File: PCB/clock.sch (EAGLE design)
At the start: 9 parts, among them IC1 74LS595N, IC2 74LS595N, IC3 74LS595N

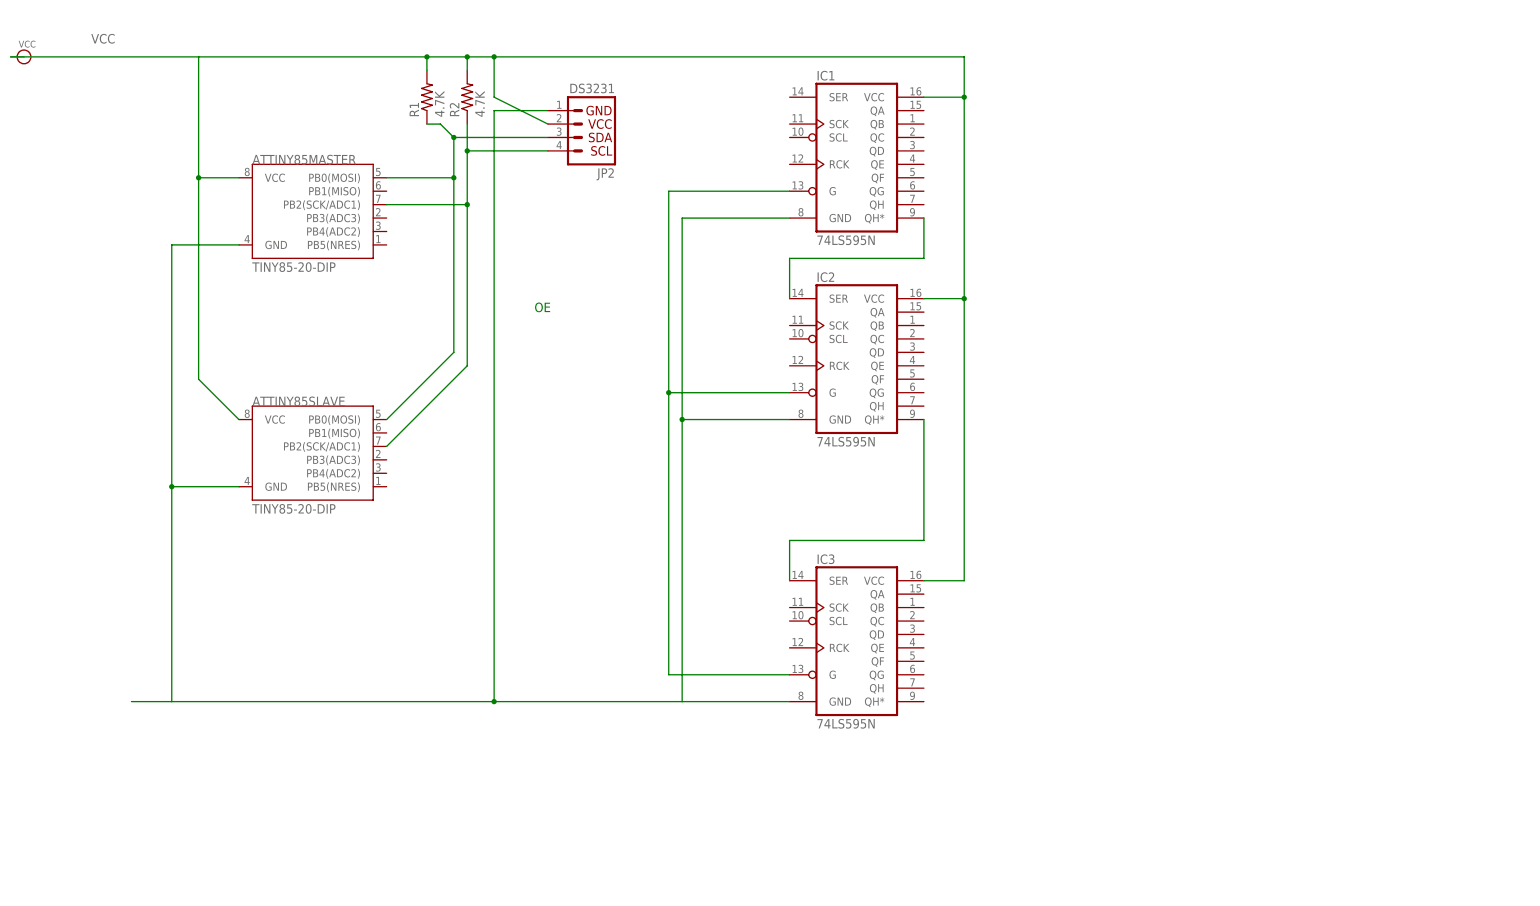
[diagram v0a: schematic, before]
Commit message: Updated the schematic for better readability
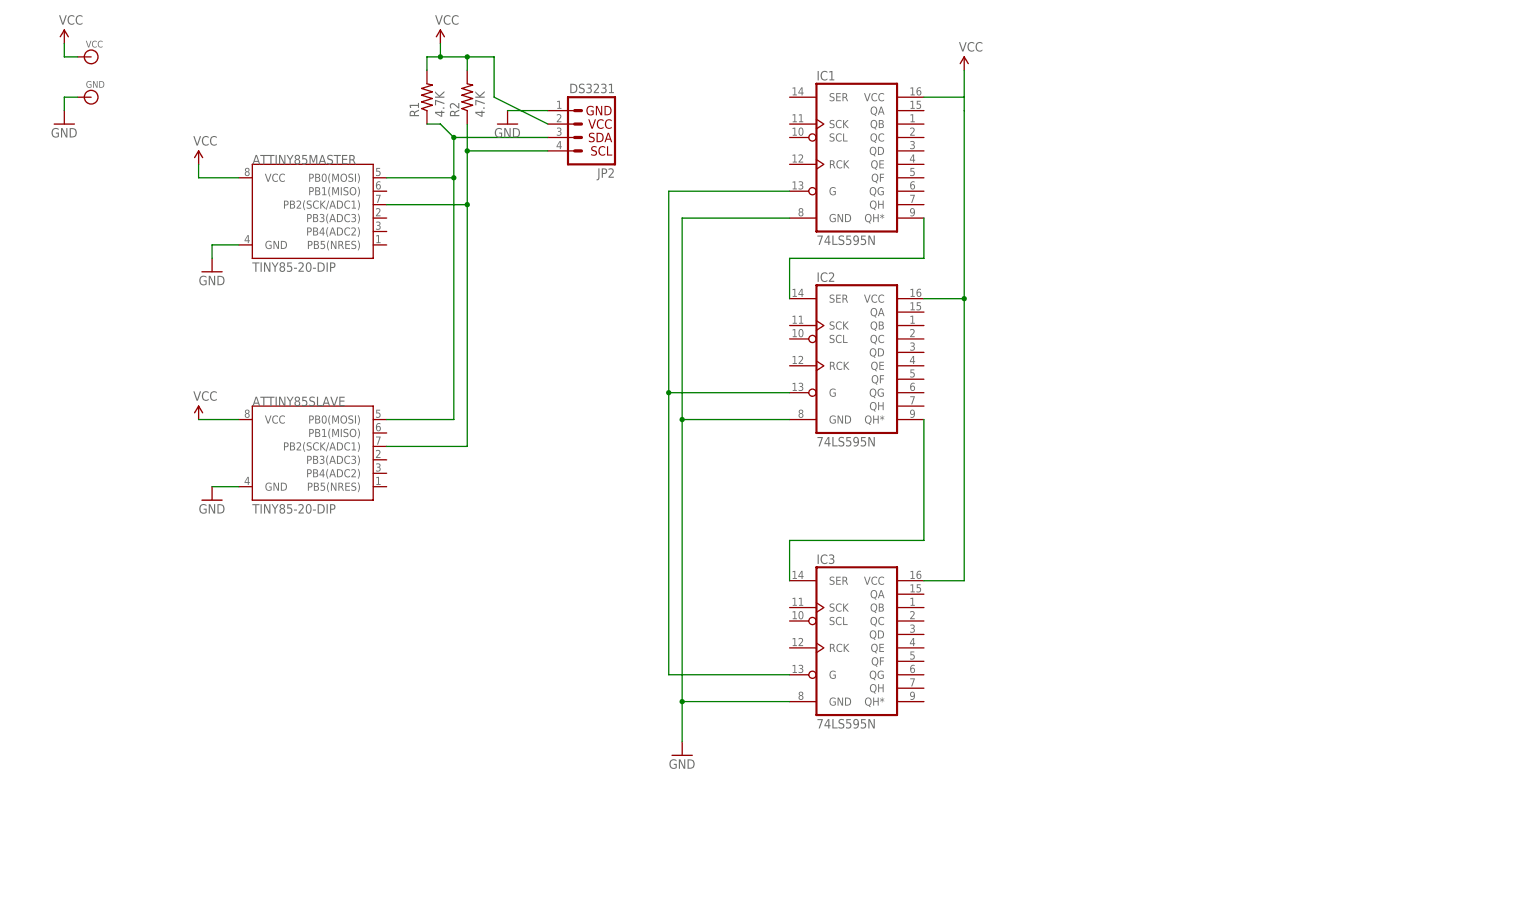
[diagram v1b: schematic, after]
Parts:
- added GND: (no value), SparkFun-Connectors:BANANA_CONN
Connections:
- net GND: now also GND.1
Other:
- note removed: "OE"
- moved on the sheet: VCC
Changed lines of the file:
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@@
 <part name="R1" library="SparkFun-Resistors" deviceset="RESISTOR" device="PTH-1/4W" value="4.7K"/>
 <part name="R2" library="SparkFun-Resistors" deviceset="RESISTOR" device="PTH-1/4W" value="4.7K"/>
+<part name="SUPPLY1" library="SparkFun-Aesthetics" deviceset="VCC" device=""/>
+<part name="SUPPLY2" library="SparkFun-Aesthetics" deviceset="VCC" device=""/>
+<part name="SUPPLY3" library="SparkFun-Aesthetics" deviceset="VCC" device=""/>
+<part name="SUPPLY4" library="SparkFun-Aesthetics" deviceset="VCC" device=""/>
+<part name="SUPPLY5" library="SparkFun-Aesthetics" deviceset="VCC" device=""/>
+<part name="GND1" library="SparkFun-Aesthetics" deviceset="GND" device=""/>
+<part name="GND2" library="SparkFun-Aesthetics" deviceset="GND" device=""/>
+<part name="GND3" library="SparkFun-Aesthetics" deviceset="GND" device=""/>
+<part name="GND4" library="SparkFun-Aesthetics" deviceset="GND" device=""/>
+<part name="GND5" library="SparkFun-Aesthetics" deviceset="GND" device=""/>
+<part name="GND" library="SparkFun-Connectors" deviceset="BANANA_CONN" device=""/>
 </parts>
 <sheets>
 <sheet>
 <plain>
-<text x="0" y="55.88" size="1.778" layer="91">OE</text>
 </plain>
 <instances>
@@
 <instance part="IC3" gate="A" x="58.42" y="-5.08"/>
 <instance part="ATTINY85MASTER" gate="G$1" x="-40.64" y="73.66"/>
-<instance part="VCC" gate="G$1" x="-96.52" y="104.14"/>
+<instance part="VCC" gate="G$1" x="-83.82" y="104.14"/>
 <instance part="JP2" gate="G$1" x="12.7" y="96.52" rot="R180"/>
 <instance part="ATTINY85SLAVE" gate="G$1" x="-40.64" y="27.94"/>
 <instance part="R1" gate="G$1" x="-20.32" y="96.52" rot="R90"/>
 <instance part="R2" gate="G$1" x="-12.7" y="96.52" rot="R90"/>
+<instance part="SUPPLY1" gate="G$1" x="-63.5" y="35.56"/>
+<instance part="SUPPLY2" gate="G$1" x="-17.78" y="106.68"/>
+<instance part="SUPPLY3" gate="G$1" x="81.28" y="101.6"/>
+<instance part="SUPPLY4" gate="G$1" x="-88.9" y="106.68"/>
+<instance part="SUPPLY5" gate="G$1" x="-63.5" y="83.82"/>
+<instance part="GND1" gate="1" x="-60.96" y="20.32"/>
+<instance part="GND2" gate="1" x="-60.96" y="63.5"/>
+<instance part="GND3" gate="1" x="-5.08" y="91.44"/>
+<instance part="GND4" gate="1" x="-88.9" y="91.44"/>
+<instance part="GND5" gate="1" x="27.94" y="-27.94"/>
+<instance part="GND" gate="G$1" x="-83.82" y="96.52"/>
 </instances>
 <busses>
@@
 <pinref part="IC1" gate="A" pin="VCC"/>
 <wire x1="73.66" y1="96.52" x2="81.28" y2="96.52" width="0.1524" layer="91"/>
-<wire x1="81.28" y1="96.52" x2="81.28" y2="58.42" width="0.1524" layer="91"/>
+<wire x1="81.28" y1="96.52" x2="81.28" y2="93.98" width="0.1524" layer="91"/>
 <junction x="81.28" y="58.42"/>
-<wire x1="81.28" y1="96.52" x2="81.28" y2="104.14" width="0.1524" layer="91"/>
-<junction x="81.28" y="96.52"/>
-<wire x1="81.28" y1="104.14" x2="-7.62" y2="104.14" width="0.1524" layer="91"/>
-<pinref part="ATTINY85MASTER" gate="G$1" pin="VCC"/>
+<pinref part="SUPPLY3" gate="G$1" pin="VCC"/>
+<wire x1="81.28" y1="93.98" x2="81.28" y2="58.42" width="0.1524" layer="91"/>
+<wire x1="81.28" y1="101.6" x2="81.28" y2="96.52" width="0.1524" layer="91"/>
+</segment>
+<segment>
+<pinref part="VCC" gate="G$1" pin="1"/>
+<pinref part="SUPPLY4" gate="G$1" pin="VCC"/>
+<wire x1="-86.36" y1="104.14" x2="-88.9" y2="104.14" width="0.1524" layer="91"/>
+<wire x1="-88.9" y1="104.14" x2="-88.9" y2="106.68" width="0.1524" layer="91"/>
+</segment>
+<segment>
+<pinref part="JP2" gate="G$1" pin="2"/>
+<wire x1="-7.62" y1="96.52" x2="2.54" y2="91.44" width="0.1524" layer="91"/>
+<wire x1="-7.62" y1="104.14" x2="-7.62" y2="96.52" width="0.1524" layer="91"/>
 <wire x1="-7.62" y1="104.14" x2="-12.7" y2="104.14" width="0.1524" layer="91"/>
-<wire x1="-12.7" y1="104.14" x2="-20.32" y2="104.14" width="0.1524" layer="91"/>
-<wire x1="-20.32" y1="104.14" x2="-63.5" y2="104.14" width="0.1524" layer="91"/>
-<wire x1="-63.5" y1="104.14" x2="-99.06" y2="104.14" width="0.1524" layer="91"/>
-<wire x1="-55.88" y1="81.28" x2="-63.5" y2="81.28" width="0.1524" layer="91"/>
-<wire x1="-63.5" y1="81.28" x2="-63.5" y2="104.14" width="0.1524" layer="91"/>
-<pinref part="VCC" gate="G$1" pin="1"/>
-<label x="-83.82" y="106.68" size="1.778" layer="95"/>
-<pinref part="JP2" gate="G$1" pin="2"/>
-<wire x1="-7.62" y1="104.14" x2="-7.62" y2="96.52" width="0.1524" layer="91"/>
-<wire x1="-7.62" y1="96.52" x2="2.54" y2="91.44" width="0.1524" layer="91"/>
-<junction x="-7.62" y="104.14"/>
-<pinref part="ATTINY85SLAVE" gate="G$1" pin="VCC"/>
-<wire x1="-63.5" y1="81.28" x2="-63.5" y2="43.18" width="0.1524" layer="91"/>
-<wire x1="-63.5" y1="43.18" x2="-55.88" y2="35.56" width="0.1524" layer="91"/>
-<junction x="-63.5" y="81.28"/>
 <pinref part="R2" gate="G$1" pin="2"/>
 <wire x1="-12.7" y1="101.6" x2="-12.7" y2="104.14" width="0.1524" layer="91"/>
 <junction x="-12.7" y="104.14"/>
+<wire x1="-12.7" y1="104.14" x2="-17.78" y2="104.14" width="0.1524" layer="91"/>
 <pinref part="R1" gate="G$1" pin="2"/>
+<wire x1="-17.78" y1="104.14" x2="-20.32" y2="104.14" width="0.1524" layer="91"/>
 <wire x1="-20.32" y1="101.6" x2="-20.32" y2="104.14" width="0.1524" layer="91"/>
-<junction x="-20.32" y="104.14"/>
+<pinref part="SUPPLY2" gate="G$1" pin="VCC"/>
+<wire x1="-17.78" y1="106.68" x2="-17.78" y2="104.14" width="0.1524" layer="91"/>
+<junction x="-17.78" y="104.14"/>
+</segment>
+<segment>
+<pinref part="ATTINY85MASTER" gate="G$1" pin="VCC"/>
+<wire x1="-55.88" y1="81.28" x2="-63.5" y2="81.28" width="0.1524" layer="91"/>
+<pinref part="SUPPLY5" gate="G$1" pin="VCC"/>
+<wire x1="-63.5" y1="83.82" x2="-63.5" y2="81.28" width="0.1524" layer="91"/>
+</segment>
+<segment>
+<pinref part="SUPPLY1" gate="G$1" pin="VCC"/>
+<pinref part="ATTINY85SLAVE" gate="G$1" pin="VCC"/>
+<wire x1="-63.5" y1="35.56" x2="-55.88" y2="35.56" width="0.1524" layer="91"/>
 </segment>
 </net>
@@
 <pinref part="IC3" gate="A" pin="GND"/>
 <wire x1="48.26" y1="-17.78" x2="27.94" y2="-17.78" width="0.1524" layer="91"/>
-<wire x1="-76.2" y1="-17.78" x2="-68.58" y2="-17.78" width="0.1524" layer="91"/>
-<wire x1="-68.58" y1="-17.78" x2="-7.62" y2="-17.78" width="0.1524" layer="91"/>
-<wire x1="-7.62" y1="-17.78" x2="27.94" y2="-17.78" width="0.1524" layer="91"/>
+<pinref part="IC2" gate="A" pin="GND"/>
 <wire x1="27.94" y1="-17.78" x2="27.94" y2="35.56" width="0.1524" layer="91"/>
-<pinref part="IC2" gate="A" pin="GND"/>
 <wire x1="27.94" y1="35.56" x2="48.26" y2="35.56" width="0.1524" layer="91"/>
 <pinref part="IC1" gate="A" pin="GND"/>
@@
 <wire x1="27.94" y1="73.66" x2="27.94" y2="35.56" width="0.1524" layer="91"/>
 <junction x="27.94" y="35.56"/>
+<pinref part="GND5" gate="1" pin="GND"/>
+<wire x1="27.94" y1="-25.4" x2="27.94" y2="-17.78" width="0.1524" layer="91"/>
+<junction x="27.94" y="-17.78"/>
+</segment>
+<segment>
+<pinref part="JP2" gate="G$1" pin="1"/>
+<pinref part="GND3" gate="1" pin="GND"/>
+<wire x1="2.54" y1="93.98" x2="-5.08" y2="93.98" width="0.1524" layer="91"/>
+</segment>
+<segment>
+<pinref part="ATTINY85SLAVE" gate="G$1" pin="GND"/>
+<wire x1="-55.88" y1="22.86" x2="-60.96" y2="22.86" width="0.1524" layer="91"/>
+<pinref part="GND1" gate="1" pin="GND"/>
+</segment>
+<segment>
 <pinref part="ATTINY85MASTER" gate="G$1" pin="GND"/>
-<wire x1="-55.88" y1="68.58" x2="-68.58" y2="68.58" width="0.1524" layer="91"/>
-<wire x1="-68.58" y1="68.58" x2="-68.58" y2="22.86" width="0.1524" layer="91"/>
-<pinref part="JP2" gate="G$1" pin="1"/>
-<wire x1="-68.58" y1="22.86" x2="-68.58" y2="-17.78" width="0.1524" layer="91"/>
-<wire x1="2.54" y1="93.98" x2="-7.62" y2="93.98" width="0.1524" layer="91"/>
-<wire x1="-7.62" y1="93.98" x2="-7.62" y2="-17.78" width="0.1524" layer="91"/>
-<junction x="-7.62" y="-17.78"/>
-<pinref part="ATTINY85SLAVE" gate="G$1" pin="GND"/>
-<wire x1="-55.88" y1="22.86" x2="-68.58" y2="22.86" width="0.1524" layer="91"/>
-<junction x="-68.58" y="22.86"/>
+<pinref part="GND2" gate="1" pin="GND"/>
+<wire x1="-55.88" y1="68.58" x2="-60.96" y2="68.58" width="0.1524" layer="91"/>
+<wire x1="-60.96" y1="68.58" x2="-60.96" y2="66.04" width="0.1524" layer="91"/>
+</segment>
+<segment>
+<pinref part="GND" gate="G$1" pin="1"/>
+<pinref part="GND4" gate="1" pin="GND"/>
+<wire x1="-86.36" y1="96.52" x2="-88.9" y2="96.52" width="0.1524" layer="91"/>
+<wire x1="-88.9" y1="96.52" x2="-88.9" y2="93.98" width="0.1524" layer="91"/>
 </segment>
 </net>
@@
 <pinref part="JP2" gate="G$1" pin="3"/>
 <pinref part="ATTINY85SLAVE" gate="G$1" pin="PB0(MOSI)"/>
-<wire x1="-15.24" y1="81.28" x2="-15.24" y2="48.26" width="0.1524" layer="91"/>
-<wire x1="-15.24" y1="48.26" x2="-27.94" y2="35.56" width="0.1524" layer="91"/>
+<wire x1="-15.24" y1="81.28" x2="-15.24" y2="35.56" width="0.1524" layer="91"/>
+<wire x1="-15.24" y1="35.56" x2="-27.94" y2="35.56" width="0.1524" layer="91"/>
 <junction x="-15.24" y="81.28"/>
 <pinref part="R1" gate="G$1" pin="1"/>
@@
 <pinref part="ATTINY85MASTER" gate="G$1" pin="PB2(SCK/ADC1)"/>
 <pinref part="ATTINY85SLAVE" gate="G$1" pin="PB2(SCK/ADC1)"/>
-<wire x1="-12.7" y1="76.2" x2="-12.7" y2="45.72" width="0.1524" layer="91"/>
-<wire x1="-12.7" y1="45.72" x2="-27.94" y2="30.48" width="0.1524" layer="91"/>
+<wire x1="-12.7" y1="76.2" x2="-12.7" y2="30.48" width="0.1524" layer="91"/>
+<wire x1="-12.7" y1="30.48" x2="-27.94" y2="30.48" width="0.1524" layer="91"/>
 <junction x="-12.7" y="76.2"/>
 <pinref part="R2" gate="G$1" pin="1"/>

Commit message: Updated the board with the darlington arrays and whatnot
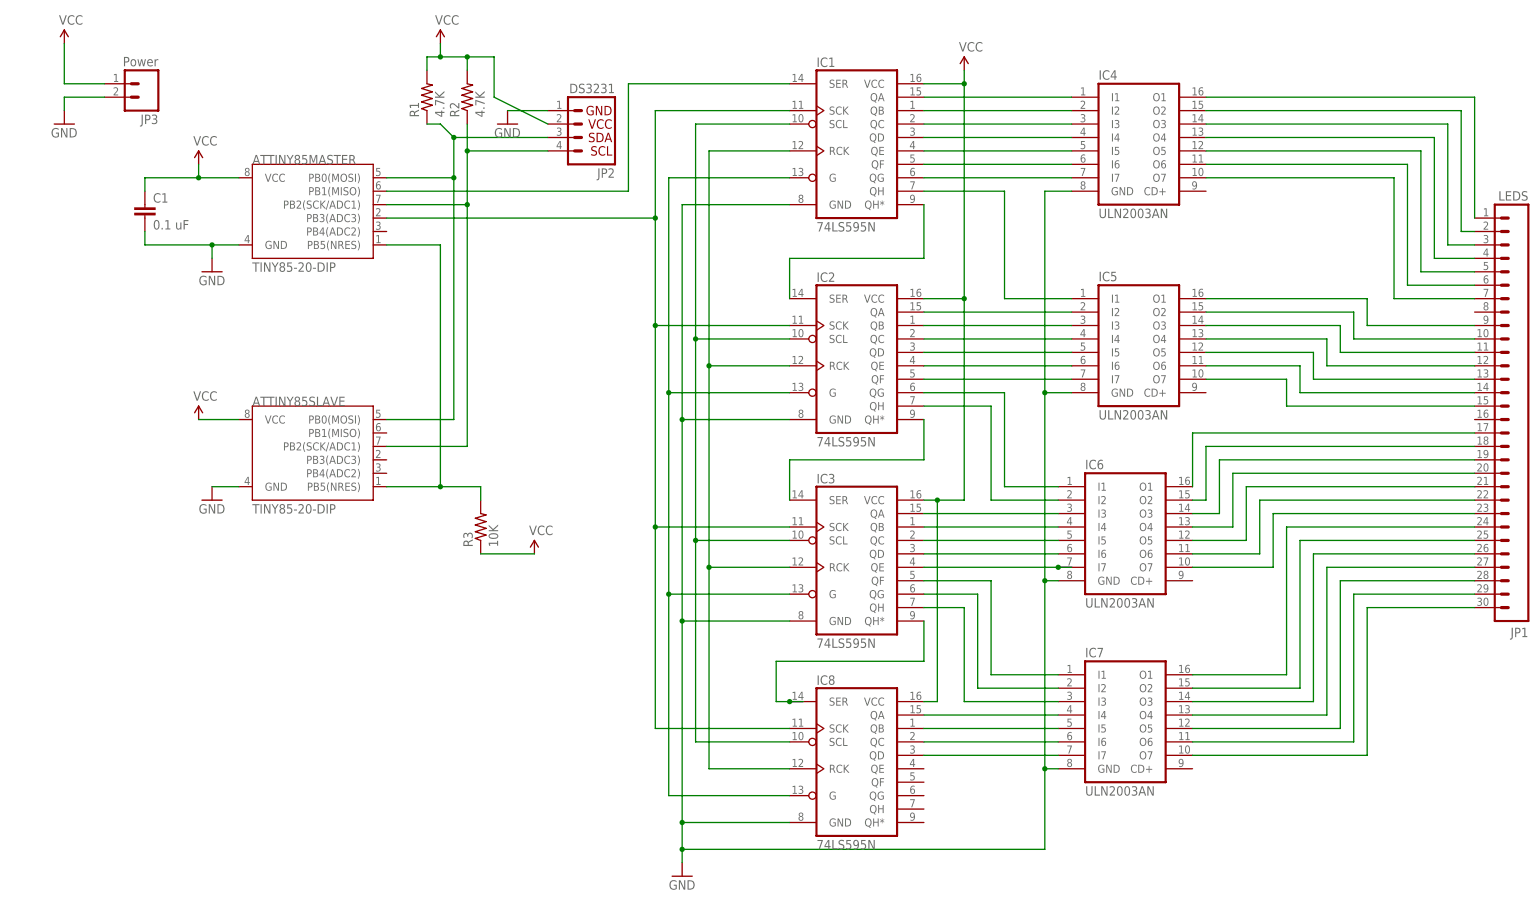
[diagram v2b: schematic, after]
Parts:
- removed GND, VCC: (no value), SparkFun-Connectors:BANANA_CONN
- added C1: 0.1 uF, SparkFun-Capacitors:CAPPTH
- added IC4, IC5, IC6, IC7: ULN2003AN, uln-udn:ULN2003AN
- added IC8: 74LS595N, SparkFun-DigitalIC:74LS595N
- added JP1: LEDS, SparkFun-Connectors:M30
- added JP3: Power, SparkFun-Connectors:M02PTH3
- added R3: 10K, SparkFun-Resistors:RESISTORPTH-1/4W
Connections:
- new net HALF: IC4.O2, JP1.2
- new net N$10: IC1.QD, IC4.I4
- new net N$11: IC1.QE, IC4.I5
- new net N$12: IC1.QF, IC4.I6
- new net N$13: IC1.QG, IC4.I7
- new net N$14: ATTINY85MASTER.PB1(MISO), IC1.SER
- new net N$15: IC1.QH, IC5.I1
- new net N$16: IC2.QA, IC5.I2
- new net N$17: IC2.QB, IC5.I3
- new net N$18: IC2.QC, IC5.I4
- new net N$19: IC2.QD, IC5.I5
- new net N$20: IC2.QE, IC5.I6
- new net N$21: IC2.QF, IC5.I7
- new net N$22: IC2.QH, IC6.I2
- new net N$23: IC2.QG, IC6.I1
- new net N$24: IC3.QA, IC6.I3
- new net N$25: IC3.QB, IC6.I4
- new net N$26: IC3.QC, IC6.I5
- new net N$27: IC3.QD, IC6.I6
- new net N$28: IC3.QE, IC6.I7
- new net N$29: IC3.QH*, IC8.SER
- new net N$30: IC7.I4, IC8.QA
- new net N$31: IC7.I5, IC8.QB
- new net N$32: IC7.I6, IC8.QC
- new net N$33: IC7.I7, IC8.QD
- new net N$34: IC3.QF, IC7.I1
- new net N$35: IC3.QG, IC7.I2
- new net N$36: IC3.QH, IC7.I3
- new net N$37: IC1.SCL, IC2.SCL, IC3.SCL, IC8.SCL
- new net N$38: IC1.RCK, IC2.RCK, IC3.RCK, IC8.RCK
- new net N$39: IC4.O3, JP1.3
- new net N$40: IC4.O4, JP1.4
- new net N$41: IC4.O5, JP1.5
- new net N$42: IC4.O6, JP1.6
- new net N$43: IC4.O7, JP1.7
- new net N$44: ATTINY85MASTER.PB3(ADC3), IC1.SCK, IC2.SCK, IC3.SCK, IC8.SCK
- new net N$45: IC5.O1, JP1.9
- new net N$46: IC5.O2, JP1.10
- new net N$47: IC5.O3, JP1.11
- new net N$48: IC5.O4, JP1.12
- new net N$49: IC5.O5, JP1.13
- new net N$50: IC5.O6, JP1.14
- new net N$51: IC5.O7, JP1.15
- new net N$52: IC7.O1, JP1.24
- new net N$53: IC6.O1, JP1.17
- new net N$54: IC6.O2, JP1.18
- new net N$55: IC6.O3, JP1.19
- new net N$56: IC6.O4, JP1.20
- new net N$57: IC6.O5, JP1.21
- new net N$58: IC6.O6, JP1.22
- new net N$59: IC6.O7, JP1.23
- new net N$6: ATTINY85MASTER.PB5(NRES), ATTINY85SLAVE.PB5(NRES), R3.2
- new net N$60: IC7.O2, JP1.25
- new net N$61: IC7.O3, JP1.26
- new net N$62: IC7.O4, JP1.27
- new net N$63: IC7.O5, JP1.28
- new net N$64: IC7.O6, JP1.29
- new net N$65: IC7.O7, JP1.30
- new net N$7: IC1.QA, IC4.I1
- new net N$8: IC1.QB, IC4.I2
- new net N$9: IC1.QC, IC4.I3
- new net TEN: IC4.O1, JP1.1
- net GND: now also C1.2, IC4.GND, IC5.GND, IC6.GND, IC7.GND, IC8.GND, JP3.2; no longer GND.1
- net N$4: now also IC8.G
- net VCC: now also C1.1, IC8.VCC, JP3.1, R3.1; no longer VCC.1
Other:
- moved on the sheet: IC1, IC3
